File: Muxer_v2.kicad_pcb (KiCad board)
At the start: 2 copper layers, 7 parts, among them J1 Conn_01x03, J2 Conn_01x06, J3 Conn_01x08

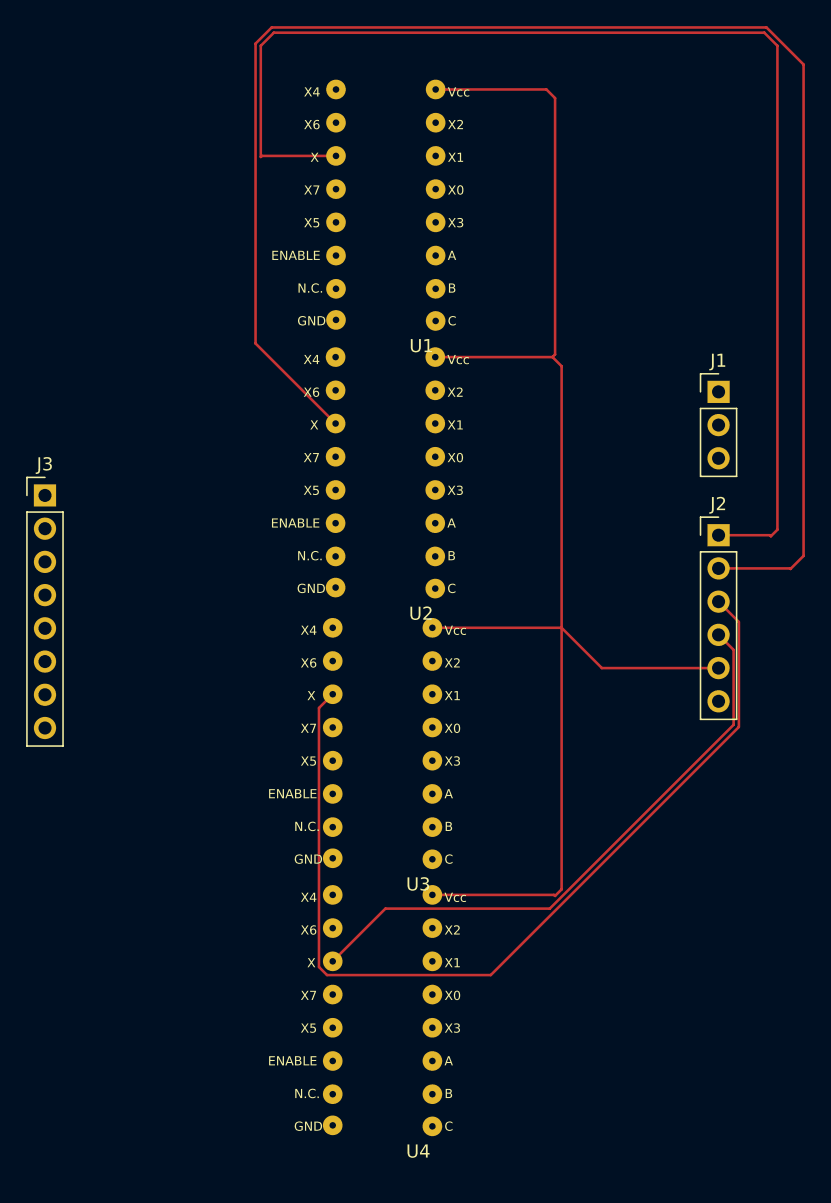
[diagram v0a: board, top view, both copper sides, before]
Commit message: Finished wiring using vias
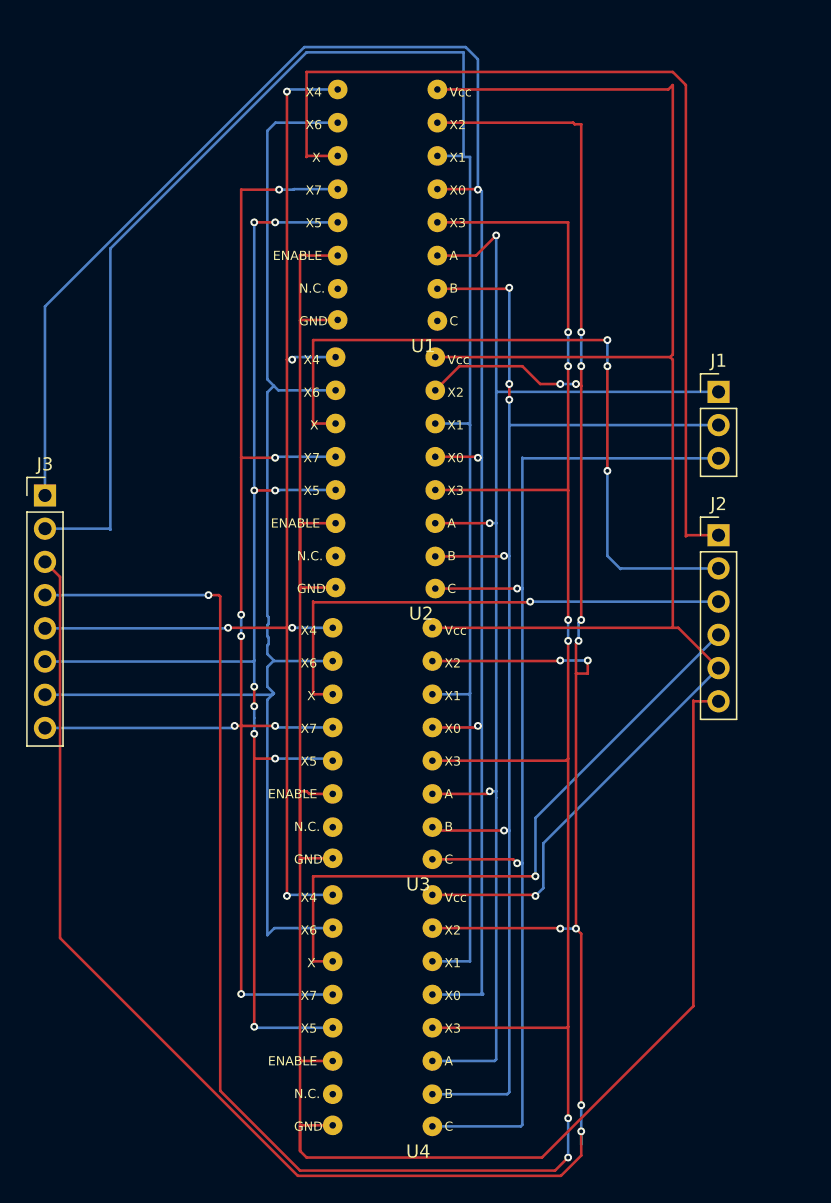
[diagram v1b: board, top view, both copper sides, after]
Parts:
- moved U1 0.13 mm to (134.9, 65.5)
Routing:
- net Net-(J3-Pin_3): track 0.00 -> 206.8 mm, vias 0 -> 12
- net Net-(J3-Pin_4): track 0.00 -> 193.4 mm, vias 0 -> 7
- net Net-(J2-GND): track 0.00 -> 162.8 mm
- net Net-(J3-Pin_1): track 0.00 -> 142.3 mm, vias 0 -> 3
- net Net-(J3-Pin_2): track 0.00 -> 140.2 mm
- net Net-(J3-Pin_8): track 0.00 -> 105.2 mm, vias 0 -> 7
- net Net-(J3-Pin_6): track 0.00 -> 102.1 mm, vias 0 -> 9
- net Net-(J1-B): track 0.00 -> 100.8 mm, vias 0 -> 5
- net Net-(J3-Pin_7): track 0.00 -> 100.6 mm
- net Net-(J1-A): track 0.00 -> 99.7 mm, vias 0 -> 3
- net Net-(J3-Pin_5): track 0.00 -> 94.7 mm, vias 0 -> 5
- net Net-(J1-C): track 0.00 -> 86.6 mm, vias 0 -> 2
- net Net-(J2-F-): track 119.7 -> 56.2 mm, vias 0 -> 3
- net Net-(J2-S+): track 71.7 -> 39.6 mm, vias 0 -> 1
- net Net-(J2-F+): track 96.4 -> 75.2 mm
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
